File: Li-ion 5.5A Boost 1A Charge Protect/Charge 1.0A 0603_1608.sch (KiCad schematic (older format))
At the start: 13 parts, among them U3 MCP73833T

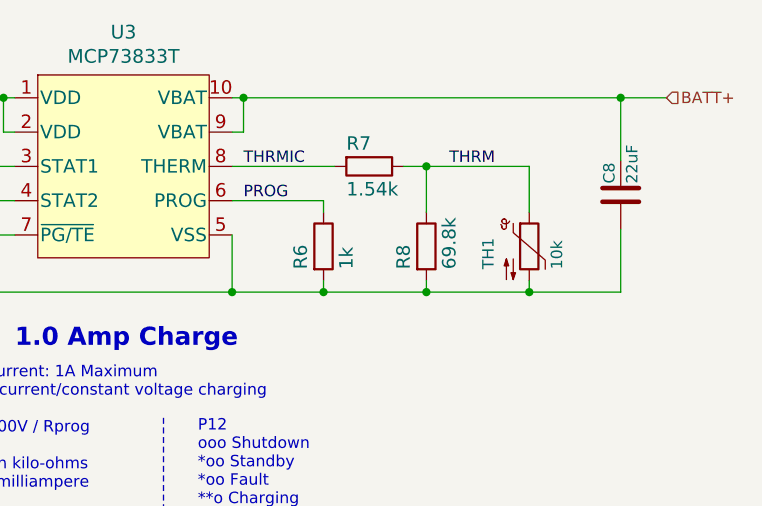
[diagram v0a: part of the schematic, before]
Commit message: Update Charge 1.0A 0603_1608.sch
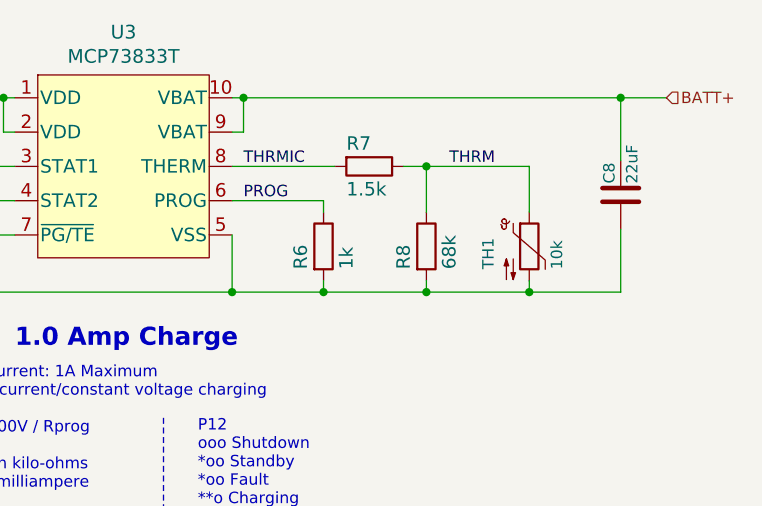
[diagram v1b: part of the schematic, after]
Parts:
- R7: value 1.54k -> 1.5k
- R8: value 69.8k -> 68k
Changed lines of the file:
@@
 P 7000 3500
 F 0 "R7" V 6900 3400 59  0000 L CNN
-F 1 "1.54k" V 7100 3400 59  0000 L CNN
+F 1 "1.5k" V 7100 3400 59  0000 L CNN
 F 2 "Frequently_Used_LE:0603_1608Metric" H 7000 3500 50  0001 C CNN
 F 3 "https://www.mouser.com/datasheet/2/348/esr_e-1139161.pdf" H 7000 3500 50  0001 C CNN
@@
 P 7250 3850
 F 0 "R8" V 7150 3750 59  0000 L CNN
-F 1 "69.8k" V 7350 3750 59  0000 L CNN
+F 1 "68k" V 7350 3750 59  0000 L CNN
 F 2 "Frequently_Used_LE:0603_1608Metric" H 7250 3850 50  0001 C CNN
 F 3 "https://www.mouser.com/datasheet/2/348/esr_e-1139161.pdf" H 7250 3850 50  0001 C CNN
